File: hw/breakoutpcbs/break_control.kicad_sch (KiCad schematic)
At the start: 21 parts, among them J11 Conn_01x07, J12 Conn_01x07, J13 Conn_01x06, J15 Conn_01x04, J16 Screw_Terminal_01x04, J17 Conn_01x05, J18 Screw_Terminal_01x04, Q10 BC337, Q11 BC847

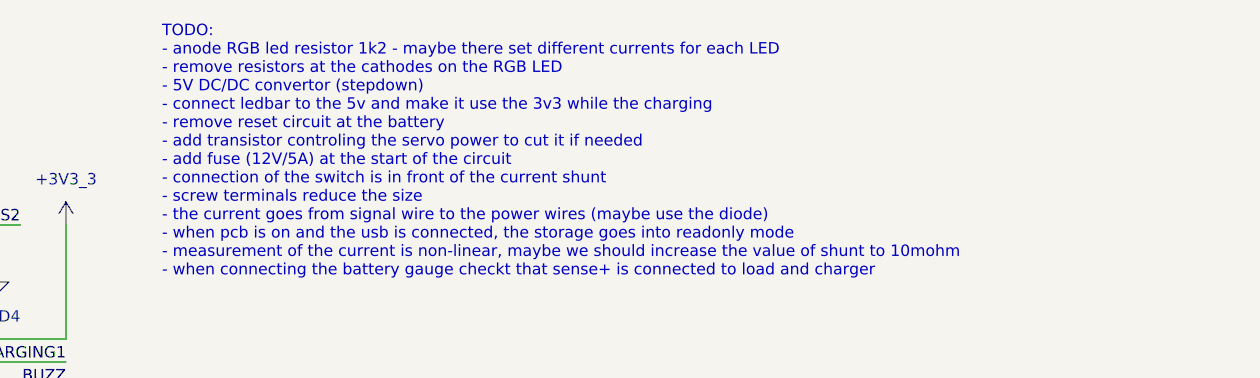
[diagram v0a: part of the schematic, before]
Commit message: moving breakout boards kicad project to hw folder including all the modules
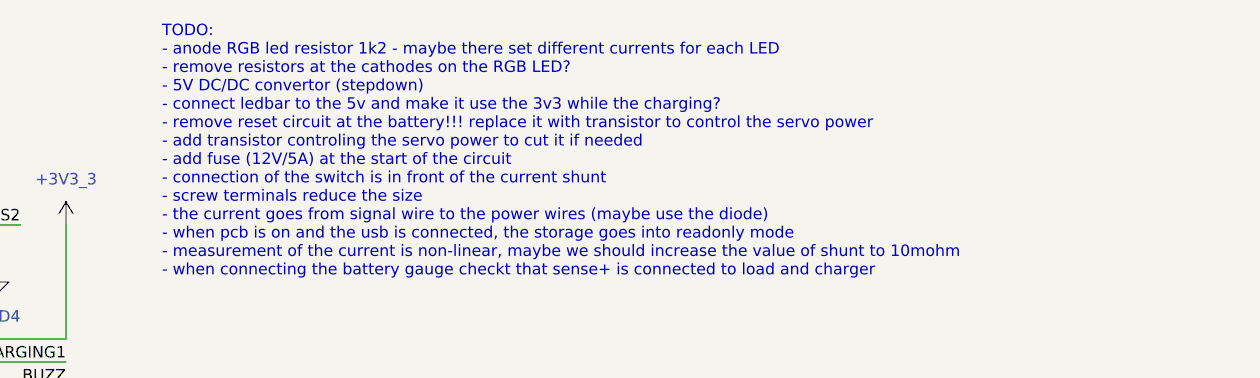
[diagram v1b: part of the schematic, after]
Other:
- note added: "TODO: - anode RGB led resistor 1k2 - maybe there set different currents for each LED - remove resistors at the cathodes on the RGB LED? - 5V DC/DC convertor (stepdown) - connect ledbar to the 5v and make it use the 3v3 while the charging? - remove reset circuit at the battery!!! replace it with transistor to control the servo power - add transistor controling the servo power to cut it if needed -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"
- note removed: "TODO: - anode RGB led resistor 1k2 - maybe there set different currents for each LED - remove resistors at the cathodes on the RGB LED - 5V DC/DC convertor (stepdown) - connect ledbar to the 5v and make it use the 3v3 while the charging - remove reset circuit at the battery - add transistor controling the servo power to cut it if needed - add fuse (12V/5A) at the start of the circuit - connection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"
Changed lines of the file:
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@@
 		)
 	)
-	(text "TODO: \n- anode RGB led resistor 1k2 - maybe there set different currents for each LED\n- remove resistors at the cathodes on the RGB LED\n- 5V DC/DC convertor (stepdown)\n- connect ledbar to the 5v and make it use the 3v3 while the charging\n- remove reset circuit at the battery\n- add transistor controling the servo power to cut it if needed\n- add fuse (12V/5A) at the start of the circuit\n- connection of the switch is in front of the current shunt\n- screw terminals reduce the size\n- the current goes from signal wire to the power wires (maybe use the diode)\n- when pcb is on and the usb is connected, the storage goes into readonly mode\n- measurement of the current is non-linear, maybe we should increase the value of shunt to 10mohm\n- when connecting the battery gauge checkt that sense+ is connected to load and charger"
+	(text "TODO: \n- anode RGB led resistor 1k2 - maybe there set different currents for each LED\n- remove resistors at the cathodes on the RGB LED?\n- 5V DC/DC convertor (stepdown)\n- connect ledbar to the 5v and make it use the 3v3 while the charging?\n- remove reset circuit at the battery!!! replace it with transistor to control the servo power\n- add transistor controling the servo power to cut it if needed\n- add fuse (12V/5A) at the start of the circuit\n- connection of the switch is in front of the current shunt\n- screw terminals reduce the size\n- the current goes from signal wire to the power wires (maybe use the diode)\n- when pcb is on and the usb is connected, the storage goes into readonly mode\n- measurement of the current is non-linear, maybe we should increase the value of shunt to 10mohm\n- when connecting the battery gauge checkt that sense+ is connected to load and charger"
 		(exclude_from_sim no)
 		(at 178.308 29.972 0)
